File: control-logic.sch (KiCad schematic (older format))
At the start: 34 parts, among them U1 STM32F072R, U2 MCP2562, X1 8.000 MHz

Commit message: I think the layout is finished now. I'll check again after I sleep.
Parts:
- removed PG1: LED, LEDs:LED-0603, symbol LED
- removed R4: 1K, Resistors_SMD:R_0603, symbol R
- C1, C2: symbol C -> C-RESCUE-score-module-pcb-v1
- C3: renamed from C8; symbol C -> C-RESCUE-score-module-pcb-v1
- C4: renamed from C9; symbol C -> C-RESCUE-score-module-pcb-v1
- C5: renamed from C3; symbol C -> C-RESCUE-score-module-pcb-v1
- C6: renamed from C4; symbol C -> C-RESCUE-score-module-pcb-v1
- C7: renamed from C5; symbol C -> C-RESCUE-score-module-pcb-v1
- C8: renamed from C6; symbol C -> C-RESCUE-score-module-pcb-v1
- C9: renamed from C7; symbol C -> C-RESCUE-score-module-pcb-v1
- R1: symbol R -> R-RESCUE-score-module-pcb-v1
- R10: renamed from R12; symbol R -> R-RESCUE-score-module-pcb-v1
- R11: renamed from R13; symbol R -> R-RESCUE-score-module-pcb-v1
- R12: renamed from R14; symbol R -> R-RESCUE-score-module-pcb-v1
- R13: renamed from R3; symbol R -> R-RESCUE-score-module-pcb-v1
- R2: renamed from R7; symbol R -> R-RESCUE-score-module-pcb-v1
- R3: renamed from R8; symbol R -> R-RESCUE-score-module-pcb-v1
- R4: renamed from R2; symbol R -> R-RESCUE-score-module-pcb-v1
- R5: renamed from R9; symbol R -> R-RESCUE-score-module-pcb-v1
- R6: renamed from R5; symbol R -> R-RESCUE-score-module-pcb-v1
- R7: renamed from R10; symbol R -> R-RESCUE-score-module-pcb-v1
- R8: renamed from R6; symbol R -> R-RESCUE-score-module-pcb-v1
- R9: renamed from R11; symbol R -> R-RESCUE-score-module-pcb-v1
- renumbered U2 to U1, U1 to U2
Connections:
- net POWER_GOOD is gone; now on net HEARTBEAT: U2.3 (PC14)
- net ADDRESS0: now also U2.51 (PC10); no longer U2.45 (PA12)
- net ADDRESS1: now also U2.52 (PC11); no longer U2.51 (PC10)
- net ADDRESS2: now also U2.53 (PC12); no longer U2.52 (PC11)
- net ADDRESS3: now also U2.54 (PD2); no longer U2.53 (PC12)
- net ADDRESS4: now also U2.55 (PB3); no longer U2.54 (PD2)
- net ADDRESS5: now also U2.2 (PC13); no longer U2.55 (PB3)
- net ADDRESS6: now also U2.57 (PB5); no longer U2.56 (PB4)
- net ADDRESS7: now also U2.56 (PB4); no longer U2.2 (PC13)
- net ANODE0: now also U2.24 (PC4)
- net ANODE1: now also U2.25 (PC5)
- net ANODE2: now also U2.26 (PB0)
- net ANODE3: now also U2.27 (PB1)
- net ANODE4: now also U2.33 (PB12)
- net ANODE5: now also U2.34 (PB13)
- net ANODE6: now also U2.35 (PB14)
- net ANODE7: now also U2.36 (PB15)
- net CATHODE0: now also U2.17 (PA3); no longer U2.44 (PA11)
- net CATHODE1: now also U2.37 (PC6); no longer U2.43 (PA10)
- net CATHODE10: now also U2.16 (PA2); no longer U2.34 (PB13)
- net CATHODE11: now also U2.15 (PA1); no longer U2.33 (PB12)
- net CATHODE12: now also U2.38 (PC7); no longer U2.30 (PB11)
- net CATHODE13: now also U2.20 (PA4); no longer U2.29 (PB10)
- net CATHODE14: now also U2.22 (PA6); no longer U2.57 (PB5)
- net CATHODE15: now also U2.14 (PA0); no longer U2.28 (PB2)
- net CATHODE16: now also U2.29 (PB10)
- net CATHODE17: now also U2.21 (PA5)
- net CATHODE18: now also U2.45 (PA12)
- net CATHODE19: now also U2.30 (PB11)
- net CATHODE3: now also U2.43 (PA10); no longer U2.41 (PA8)
- net CATHODE4: now also U2.44 (PA11); no longer U2.40 (PC9)
- net CATHODE5: now also U2.41 (PA8); no longer U2.39 (PC8)
- net CATHODE6: now also U2.23 (PA7); no longer U2.38 (PC7)
- net CATHODE7: now also U2.28 (PB2); no longer U2.37 (PC6)
- net CATHODE8: now also U2.40 (PC9); no longer U2.36 (PB15)
- net CATHODE9: now also U2.39 (PC8); no longer U2.35 (PB14)
- net HEARTBEAT: now also HB1.2 (A); no longer HB1.1 (K), U2.4 (PC15)
- net at R13.1: now also HB1.1 (K); no longer HB1.2 (A)
- no-connect marks 0 -> 4

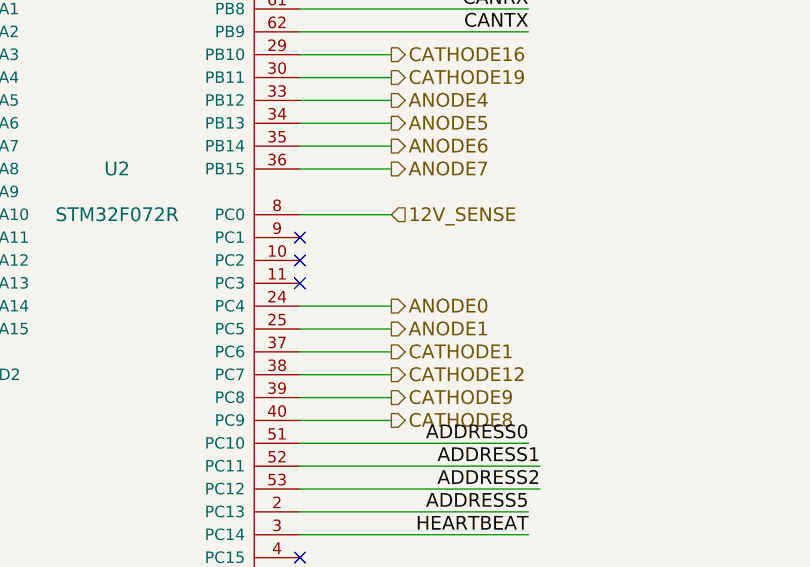
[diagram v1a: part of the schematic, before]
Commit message: Adding RGB LED driver
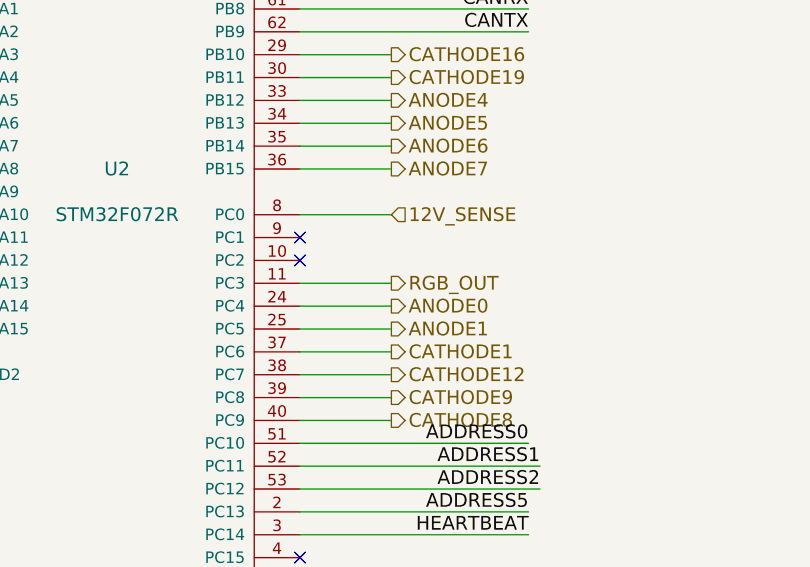
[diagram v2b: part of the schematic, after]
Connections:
- net RGB_OUT: now reaches U2.11 (PC3)
- no-connect marks 4 -> 3
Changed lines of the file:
@@
 $Descr USLetter 11000 8500
 encoding utf-8
-Sheet 2 7
+Sheet 2 8
 Title "DIYPinball Score Display Module"
 Date "Tuesday, August 04, 2015"
@@
 Wire Wire Line
 	5050 4800 4050 4800
-NoConn ~ 4050 3700
+Text HLabel 4450 3700 2    60   Output ~ 0
+RGB_OUT
+Wire Wire Line
+	4450 3700 4050 3700
 $EndSCHEMATC
